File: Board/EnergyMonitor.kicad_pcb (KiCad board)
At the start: 2 copper layers, 100 x 87 mm, 56 parts, among them J2 RPi Zero, J3 Display, J4 Screw_Terminal_01x12, J5 Screw_Terminal_01x03, Q1 BSS138, Q2 BSS138, U1 MCP3424, U2 MCP3424, U3 WE-TVS-824014, U4 WE-TVS-824014

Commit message: fully routed pcb
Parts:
- added REF**: OSHW-Logo2_14.6x12mm_Copper, Symbol:OSHW-Logo2_14.6x12mm_Copper, F.Cu at (191.5, 55.6)
- added REF**: Symbol_CreativeCommons_CopperTop_Type2_Big, Symbol:Symbol_CreativeCommons_CopperTop_Type2_Big, F.Cu at (191.5, 127.3)
- added REF**: Symbol_CC-ShareAlike_CopperTop_Small, Symbol:Symbol_CC-ShareAlike_CopperTop_Small, F.Cu at (196.1, 117.9)
- added REF**: Symbol_Attention_CopperTop_Small, Symbol:Symbol_Attention_CopperTop_Small, F.Cu at (167.4, 129.5)
- added REF**: Symbol_CC-Attribution_CopperTop_Small, Symbol:Symbol_CC-Attribution_CopperTop_Small, F.Cu at (196.1, 111.8)
- added REF**: Symbol_CreativeCommons_SilkScreenTop_Type2_Big, Symbol:Symbol_CreativeCommons_SilkScreenTop_Type2_Big, F.Cu at (191.5, 127.3)
- added REF**: OSHW-Logo2_14.6x12mm_SilkScreen, Symbol:OSHW-Logo2_14.6x12mm_SilkScreen, F.Cu at (191.5, 55.6)
- added kibuzzard-6249901A: G***, kibuzzard-6249901A, F.Cu at (138.9, 119.6)
- added kibuzzard-62499035: G***, kibuzzard-62499035, F.Cu at (145.5, 119.6)
- added kibuzzard-624990CE: G***, kibuzzard-624990CE, F.Cu at (152.4, 119.6)
- added kibuzzard-624991A3: G***, kibuzzard-624991A3, F.Cu at (110.0, 121.2)
- added kibuzzard-624991BE: G***, kibuzzard-624991BE, F.Cu at (170.7, 108.2)
- added kibuzzard-624992C2: G***, kibuzzard-624992C2, F.Cu at (134.4, 68.6)
- added kibuzzard-624992EE: G***, kibuzzard-624992EE, F.Cu at (125.5, 111.3)
- added kibuzzard-62499525: G***, kibuzzard-62499525, F.Cu at (135.9, 73.2)
- added kibuzzard-62499532: G***, kibuzzard-62499532, F.Cu at (127.3, 73.2)
- added kibuzzard-6249A574: G***, kibuzzard-6249A574, F.Cu at (105.8, 77.5)
- added kibuzzard-6249A738: G***, kibuzzard-6249A738, F.Cu at (113.8, 60.0)
- added kibuzzard-6249A748: G***, kibuzzard-6249A748, F.Cu at (123.8, 60.0)
- added kibuzzard-6249A75F: G***, kibuzzard-6249A75F, F.Cu at (133.9, 59.9)
- added kibuzzard-6249A773: G***, kibuzzard-6249A773, F.Cu at (143.8, 59.9)
- added kibuzzard-6249A77E: G***, kibuzzard-6249A77E, F.Cu at (153.9, 59.9)
- added kibuzzard-6249A788: G***, kibuzzard-6249A788, F.Cu at (163.8, 59.9)
- added kibuzzard-6249A794: G***, kibuzzard-6249A794, F.Cu at (159.0, 59.9)
- added kibuzzard-6249A794: G***, kibuzzard-6249A794, F.Cu at (128.8, 59.9)
- added kibuzzard-6249A794: G***, kibuzzard-6249A794, F.Cu at (138.9, 59.9)
- added kibuzzard-6249A794: G***, kibuzzard-6249A794, F.Cu at (109.0, 59.9)
- added kibuzzard-6249A794: G***, kibuzzard-6249A794, F.Cu at (148.8, 59.9)
- added kibuzzard-6249A794: G***, kibuzzard-6249A794, F.Cu at (118.9, 59.9)
- added kibuzzard-6249ABCA: G***, kibuzzard-6249ABCA, F.Cu at (191.8, 91.2)
- moved U4 8.64 mm to (167.4, 60.2)
- moved U3 4.45 mm to (131.7, 64.6)
- moved TR1 1.94 mm to (170.9, 107.5)
- moved R1 1.12 mm to (170.9, 81.4)
- moved JP2 1.02 mm to (138.8, 78.7)
- moved R3 1.02 mm to (176.3, 81.4)
- moved Q2 1.02 mm to (135.6, 78.7)
- moved R6 1.02 mm to (135.6, 82.5)
- moved R8 1.02 mm to (135.6, 74.9)
- moved JP4 0.78 mm to (166.6, 82.8)
- moved C3 0.76 mm to (120.7, 72.9), turned to -90 degrees
- turned C8 to 90 degrees
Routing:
- net ADC CH5: track 20.3 -> 29.0 mm
- net ADC CH3: track 29.3 -> 33.5 mm
- net ADC CH2: track 39.3 -> 43.3 mm
- net Net-(R1-Pad1): track 37.1 -> 33.4 mm
- net ADC CH4: track 30.3 -> 32.6 mm
- net Net-(C1-Pad1): track 58.9 -> 56.7 mm
- net ADC CH1: track 57.7 -> 59.8 mm
- net LINE: track 61.0 -> 63.0 mm
- net ADC CH7: track 6.14 -> 4.92 mm
- net NEUT: track 93.1 -> 94.2 mm
- net +3V3: track 43.8 -> 44.8 mm
- net SCLL: track 12.2 -> 13.1 mm
- net +5V: track 93.5 -> 92.8 mm
- net SCLH: track 68.6 -> 69.1 mm
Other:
- board text added: "Rev. 1 github.com/dangrie158/Energy-Monitor"

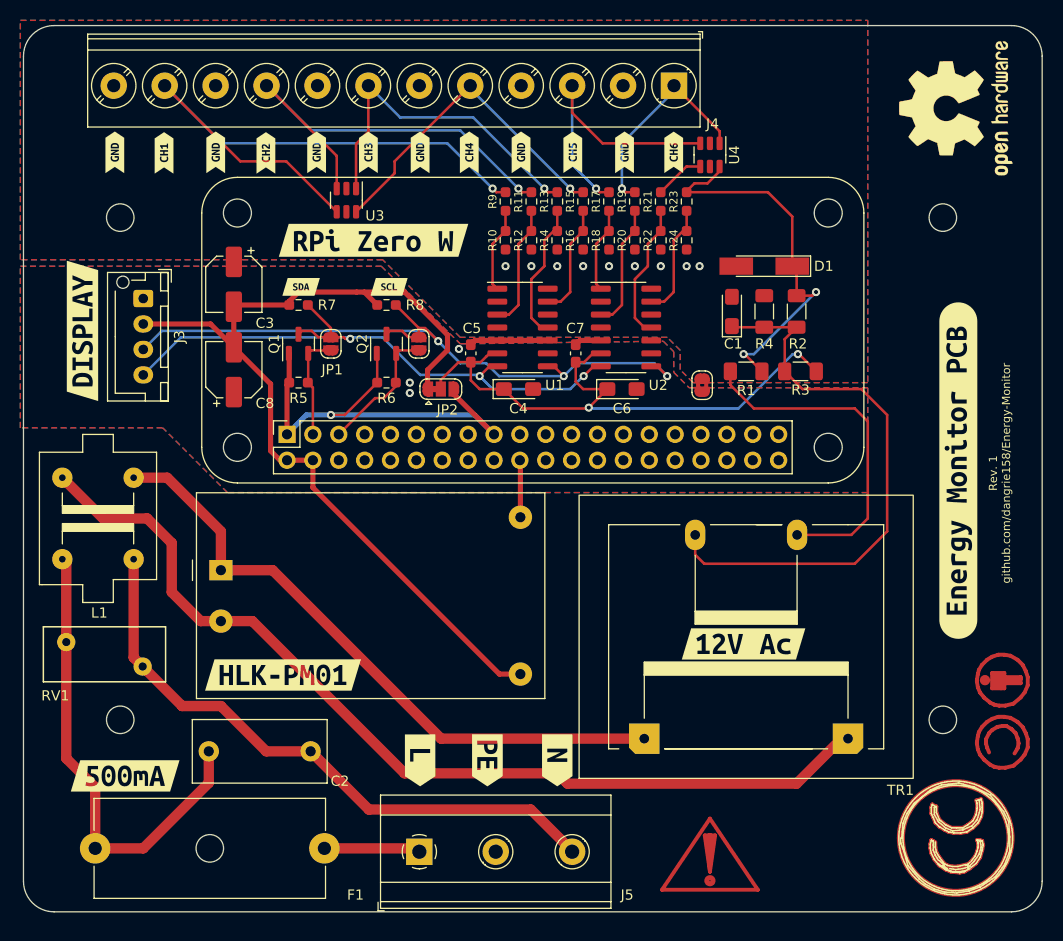
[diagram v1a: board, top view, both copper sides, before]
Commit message: resized PCB slightly for a better fit in the case
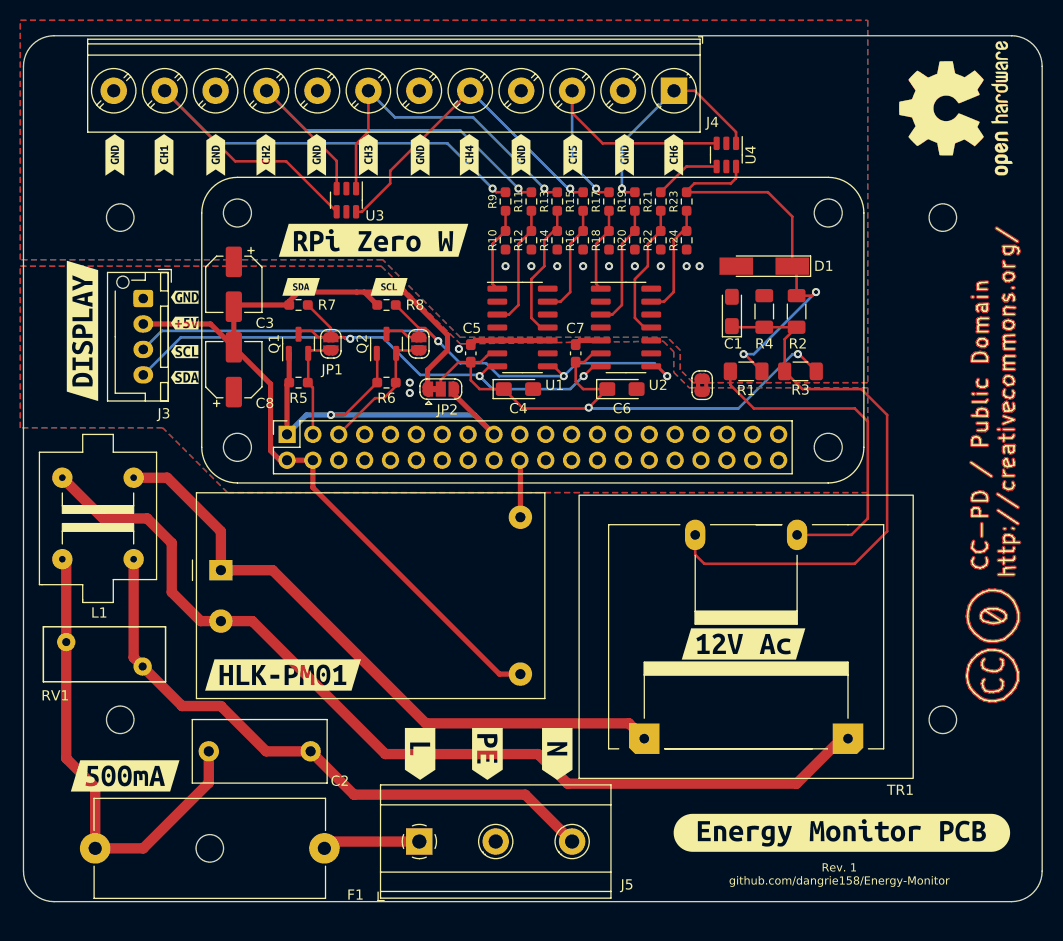
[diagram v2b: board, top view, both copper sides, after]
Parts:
- removed the REF** at (191.5, 127.3) (x2)
- removed the REF** at (196.1, 117.9)
- removed the REF** at (167.4, 129.5)
- removed the REF** at (196.1, 111.8)
- added REF**: Symbol_CreativeCommonsPublicDomain_SilkScreenTop_Small, Symbol:Symbol_CreativeCommonsPublicDomain_SilkScreenTop_Small, F.Cu at (195.1, 91.7)
- added REF**: Symbol_CreativeCommonsPublicDomain_CopperTop_Small, Symbol:Symbol_CreativeCommonsPublicDomain_CopperTop_Small, F.Cu at (195.1, 91.7)
- added kibuzzard-6249B420: G***, kibuzzard-6249B420, F.Cu at (115.8, 76.7)
- added kibuzzard-6249B42C: G***, kibuzzard-6249B42C, F.Cu at (115.8, 74.2)
- added kibuzzard-6249B43B: G***, kibuzzard-6249B43B, F.Cu at (115.8, 79.5)
- added kibuzzard-6249B447: G***, kibuzzard-6249B447, F.Cu at (115.8, 82.0)
- moved kibuzzard-6249ABCA 37.4 mm to (180.3, 126.7), turned to 0 degrees
- moved U4 1.61 mm to (169.0, 60.2)
- moved J5 1.00 mm to (138.9, 127.6)
- moved kibuzzard-6249901A 0.63 mm to (138.9, 119.0)
- moved kibuzzard-62499035 0.63 mm to (145.5, 119.0)
- moved kibuzzard-624990CE 0.63 mm to (152.4, 119.0)
- moved J4 0.50 mm to (163.9, 53.9)
- moved kibuzzard-6249A75F 0.25 mm to (133.9, 60.2)
- moved kibuzzard-6249A773 0.25 mm to (143.8, 60.2)
- moved kibuzzard-6249A77E 0.25 mm to (153.9, 60.2)
- moved kibuzzard-6249A788 0.25 mm to (163.8, 60.2)
- moved kibuzzard-6249A794 0.25 mm to (159.0, 60.2)
- moved kibuzzard-6249A794 0.25 mm to (128.8, 60.2)
- moved kibuzzard-6249A794 0.25 mm to (138.9, 60.2)
- moved kibuzzard-6249A794 0.25 mm to (109.0, 60.2)
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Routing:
- net ADC CH8: track 38.1 -> 40.1 mm
- net ADC CH7: track 4.92 -> 6.53 mm
- net ADC CH6: track 21.1 -> 22.0 mm
- net ADC CH3: track 33.5 -> 32.8 mm
- net ADC CH2: track 43.3 -> 42.6 mm
- net ADC CH5: track 29.0 -> 29.6 mm
- net ADC CH4: track 32.6 -> 32.1 mm
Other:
- board size 100 x 87 mm -> 100 x 85 mm

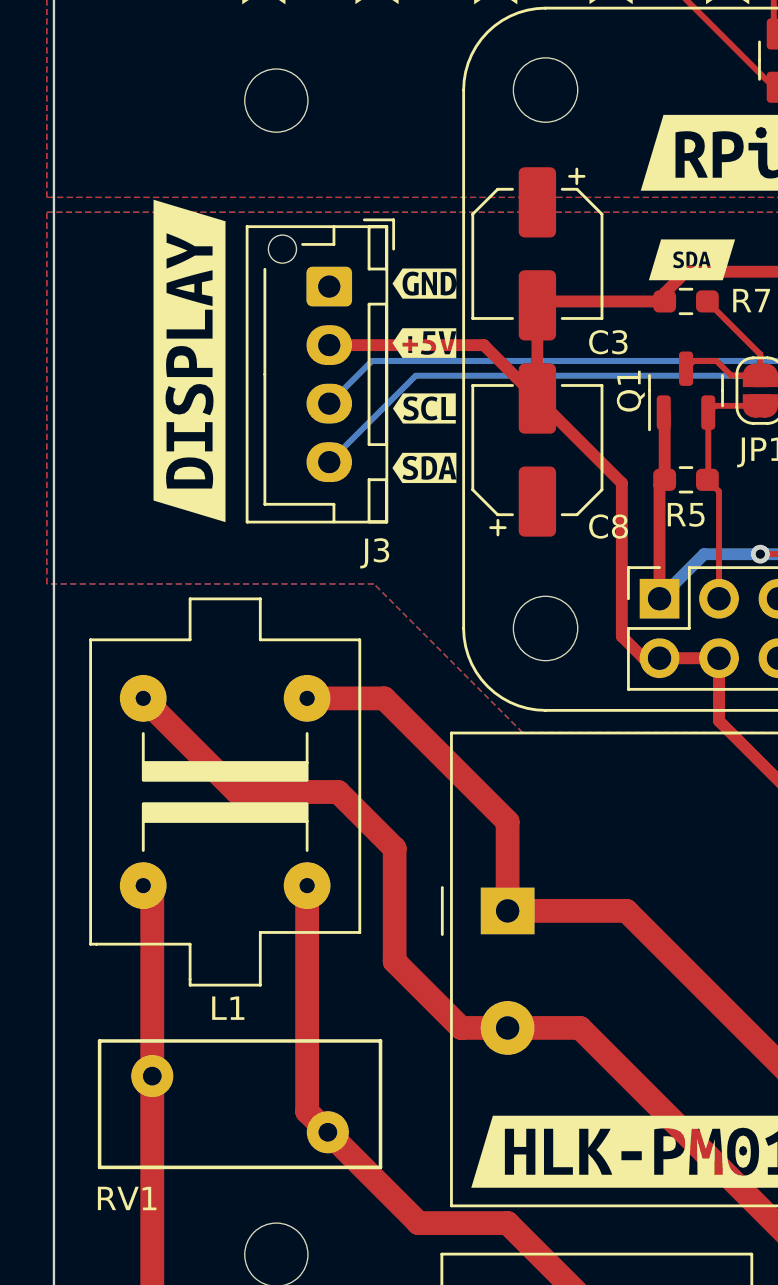
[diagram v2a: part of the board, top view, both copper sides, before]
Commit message: fixed some board layout issues after prototype assembly
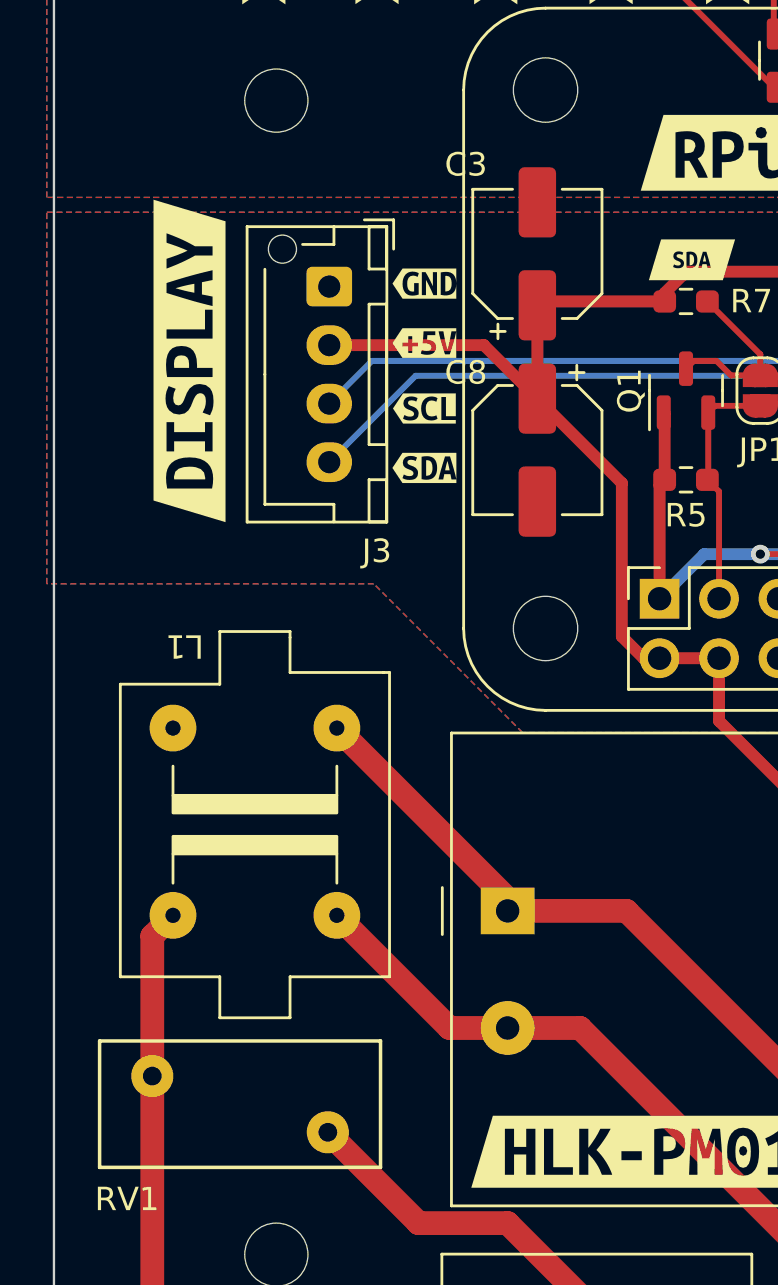
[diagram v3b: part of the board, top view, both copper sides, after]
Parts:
- J5: value Screw_Terminal_01x03 -> AC In
- R3, R4: value 470k -> 100k
- moved L1 1.80 mm to (108.6, 97.2), turned to 180 degrees
- turned C3 to 90 degrees
- turned C8 to -90 degrees
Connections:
- C3 pad 1: GND -> +5V
- C3 pad 2: +5V -> GND
- C8 pad 1: GND -> +5V
- C8 pad 2: +5V -> GND
- L1 pad 1: Net-(C2-Pad2) -> NEUT
- L1 pad 2: Net-(C2-Pad1) -> LINE
- L1 pad 3: LINE -> Net-(C2-Pad1)
- L1 pad 4: NEUT -> Net-(C2-Pad2)
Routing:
- net NEUT: track 94.2 -> 79.3 mm
- net Net-(C2-Pad1): track 60.2 -> 49.3 mm
- net LINE: track 63.0 -> 59.2 mm
- net Net-(C2-Pad2): track 46.6 -> 45.6 mm

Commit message: updated board to match updated schematic
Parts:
- R3: value 100k -> DNP
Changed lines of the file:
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@@
       (effects (font (size 1 1) (thickness 0.15)))
     )
-    (fp_text value "100k" (at 0 1.82) (layer "F.Fab")
+    (fp_text value "DNP" (at 0 1.82) (layer "F.Fab")
       (effects (font (size 1 1) (thickness 0.15)))
     )
